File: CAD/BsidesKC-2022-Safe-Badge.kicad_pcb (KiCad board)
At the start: 2 copper layers, 104.1 x 121.5 mm, 7 parts

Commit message: WIP
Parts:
- removed the G*** at (0.00, 0.00) (x7)
- added G***: LOGO, LOGO, F.Cu at (12.8, 19.2)
- added G*** (x4): LOGO, LOGO, F.Cu at (147.9, 84.0)
- added G***: LOGO, LOGO, F.Cu at (21.1, 18.9)
- added G***: LOGO, LOGO, F.Cu at (19.1, 22.8)
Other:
- net class Default removed

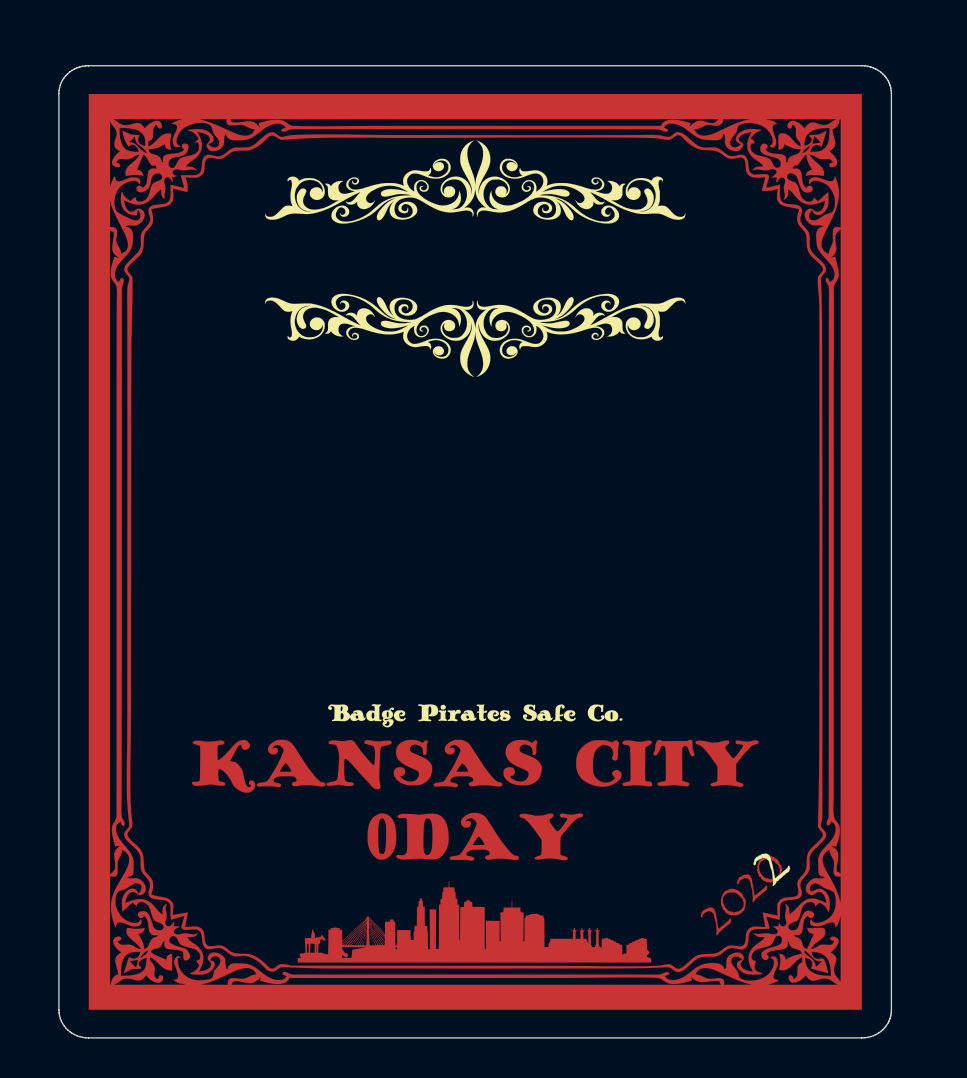
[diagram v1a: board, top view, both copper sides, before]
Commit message: adding and taking away
Adding electronics to boards, and removing old builds.
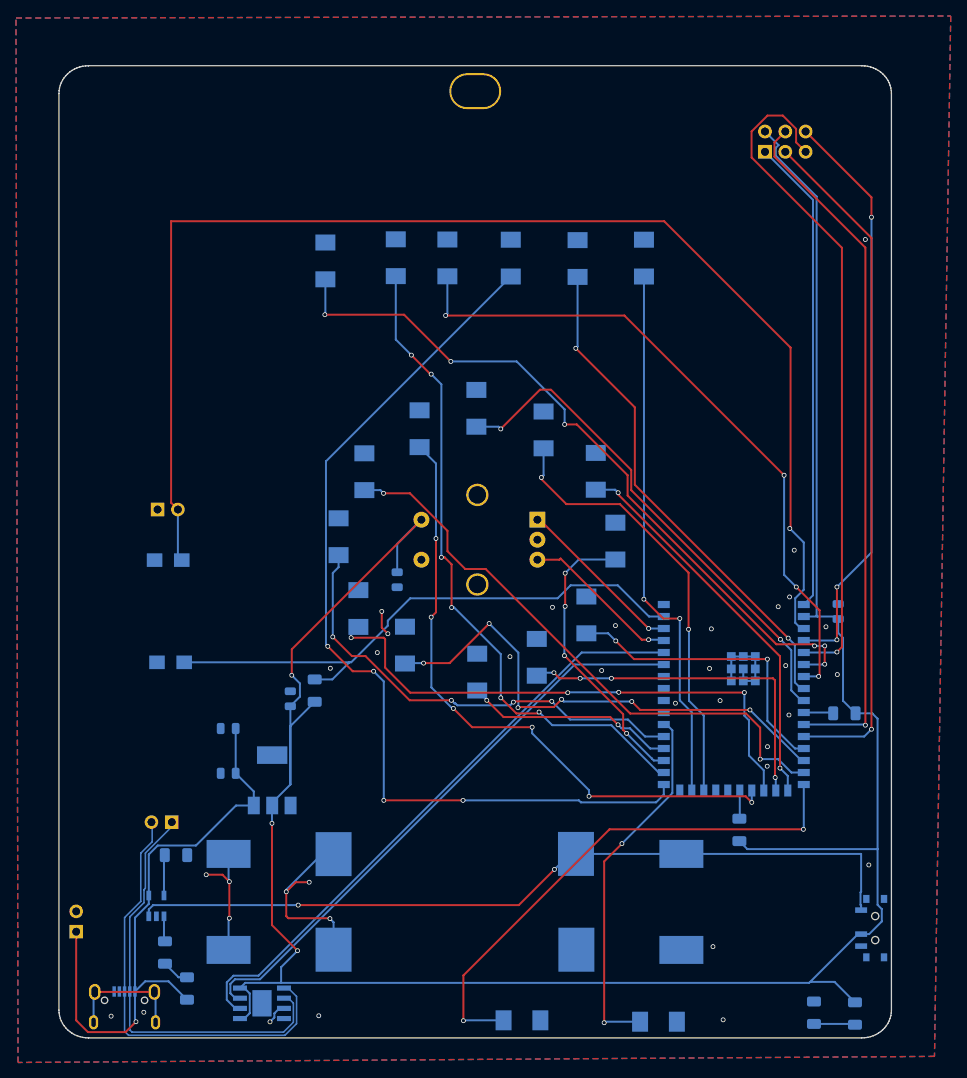
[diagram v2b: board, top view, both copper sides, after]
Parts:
- removed the G*** at (147.9, 84.0) (x2)
- added 1/0: SW_SPDT, BadgePiratesCommon:SW_SPDT_PCM12, B.Cu at (197.8, 135.3)
- added BT1: Battery, BadgePiratesCommon:AA, B.Cu at (145.6, 129.1)
- added C1: 1uF, BadgePiratesCommon:C_0805_2012Metric, B.Cu at (117.2, 110.4)
- added C2: 22uF, BadgePiratesCommon:C_0805_2012Metric, B.Cu at (193.4, 95.8)
- added C3: 0.1uF, BadgePiratesCommon:C_0805_2012Metric, B.Cu at (125.0, 106.7)
- added C4: .1uF, BadgePiratesCommon:C_0805_2012Metric, B.Cu at (138.3, 91.8)
- added C5: .1uF, BadgePiratesCommon:C_0805_2012Metric, B.Cu at (117.2, 116.0)
- added D- D+: Conn_01x02_Female, BadgePiratesCommon:PinHeader_1x02_P2.54mm_Vertical, B.Cu at (110.2, 122.1)
- added D1: LED, BadgePiratesCommon:LED_Osram_Lx_P47F_D2mm_ReverseMount_Proper_Mask Only, F.Cu at (129.3, 52.0)
- added D10: LED, BadgePiratesCommon:LED_Osram_Lx_P47F_D2mm_ReverseMount_Proper_Mask Only, F.Cu at (165.6, 87.0)
- added D11: LED, BadgePiratesCommon:LED_Osram_Lx_P47F_D2mm_ReverseMount_Proper_Mask Only, F.Cu at (162.0, 96.2)
- added D12: Charging LED, LED_SMD:LED_1206_3216Metric, B.Cu at (112.0, 142.9)
- added D13: LED, BadgePiratesCommon:LED_Osram_Lx_P47F_D2mm_ReverseMount_Proper_Mask Only, F.Cu at (155.8, 101.5)
- added D14: LED, BadgePiratesCommon:LED_Osram_Lx_P47F_D2mm_ReverseMount_Proper_Mask Only, F.Cu at (148.3, 103.3)
- added D15: LED, BadgePiratesCommon:LED_Osram_Lx_P47F_D2mm_ReverseMount_Proper_Mask Only, F.Cu at (139.3, 100.0)
- added D16: Pwr, LED_SMD:LED_1206_3216Metric, B.Cu at (190.4, 145.9)
- added D17: LED, BadgePiratesCommon:LED_Osram_Lx_P47F_D2mm_ReverseMount_Proper_Mask Only, F.Cu at (133.5, 95.4)
- added D18: LED, BadgePiratesCommon:LED_Osram_Lx_P47F_D2mm_ReverseMount_Proper_Mask Only, F.Cu at (131.0, 86.4)
- added D19: LED, BadgePiratesCommon:LED_Osram_Lx_P47F_D2mm_ReverseMount_Proper_Mask Only, F.Cu at (134.2, 78.3)
- added D2: LED, BadgePiratesCommon:LED_Osram_Lx_P47F_D2mm_ReverseMount_Proper_Mask Only, F.Cu at (138.2, 51.5)
- added D20: LED, BadgePiratesCommon:LED_Osram_Lx_P47F_D2mm_ReverseMount_Proper_Mask Only, F.Cu at (141.1, 72.9)
- added D21: LED, BadgePiratesCommon:LED_Osram_Lx_P47F_D2mm_ReverseMount_Proper_Mask Only, F.Cu at (171.0, 147.1)
- added D22: LED, BadgePiratesCommon:LED_Osram_Lx_P47F_D2mm_ReverseMount_Proper_Mask Only, F.Cu at (153.9, 146.9)
- added D3: LED, BadgePiratesCommon:LED_Osram_Lx_P47F_D2mm_ReverseMount_Proper_Mask Only, F.Cu at (144.6, 51.6)
- added D4: LED, BadgePiratesCommon:LED_Osram_Lx_P47F_D2mm_ReverseMount_Proper_Mask Only, F.Cu at (152.5, 51.6)
- added D5: LED, BadgePiratesCommon:LED_Osram_Lx_P47F_D2mm_ReverseMount_Proper_Mask Only, F.Cu at (160.9, 51.6)
- added D6: LED, BadgePiratesCommon:LED_Osram_Lx_P47F_D2mm_ReverseMount_Proper_Mask Only, F.Cu at (169.2, 51.6)
- added D7: LED, BadgePiratesCommon:LED_Osram_Lx_P47F_D2mm_ReverseMount_Proper_Mask Only, F.Cu at (148.2, 70.4)
- added D8: LED, BadgePiratesCommon:LED_Osram_Lx_P47F_D2mm_ReverseMount_Proper_Mask Only, F.Cu at (156.6, 73.1)
- added D9: LED, BadgePiratesCommon:LED_Osram_Lx_P47F_D2mm_ReverseMount_Proper_Mask Only, F.Cu at (163.2, 78.2)
- added ESP32-S2 ROVER: ESP32-S2-WROVER, BadgePiratesCommon:ESP32-S2-WROVER, B.Cu at (180.4, 106.0)
- added G***: LOGO, BadgePirateLogos:BadgePiratesURL_B.SLK, F.Cu at (101.6, 52.8)
- added G***: LOGO, BadgePirateLogos:shi%%y_B.SLK, F.Cu at (195.8, 41.4)
- added G***: fg, BadgePirateLogos:FG_B.SILK, F.Cu at (132.0, 39.0)
- added G***: pecord, BadgePirateLogos:pecord_B.SLK, F.Cu at (155.0, 40.5)
- added G***: NG_BSilk, BadgePirateLogos:NG_B.SLK, F.Cu at (167.5, 38.0)
- added G***: JiggleBilly, BadgePirateLogos:Jiggle_B.SLK, F.Cu at (143.2, 39.9)
- added G***: BP Logo, BadgePirateLogos:BPSkull_Distressed_B.SILK, F.Cu at (103.8, 36.8)
- added GND 5v: Conn_01x02_Female, BadgePiratesCommon:PinHeader_1x02_P2.54mm_Vertical, B.Cu at (98.2, 135.8)
- added J2: Conn_01x02_Female, BadgePiratesCommon:PinHeader_1x02_P2.54mm_Vertical, B.Cu at (108.4, 83.0)
- added J4: USB_B_Mini, BadgePiratesCommon:USB_Micro-B_Wuerth, B.Cu at (104.2, 145.2)
- added R1: 2k, BadgePiratesCommon:R_1206_3216Metric, B.Cu at (110.7, 126.2)
- added R2: 330, BadgePiratesCommon:R_1206_3216Metric, B.Cu at (109.3, 138.4)
- added R3: R, BadgePiratesCommon:R_1206_3216Metric, B.Cu at (195.6, 146.0)
- added R4: 1k, BadgePiratesCommon:R_1206_3216Metric, B.Cu at (128.0, 105.7)
- added R5: 10k, BadgePiratesCommon:R_1206_3216Metric, B.Cu at (181.1, 123.1)
- added R6: R_Small_US, BadgePiratesCommon:R_1206_3216Metric, B.Cu at (194.2, 108.5)
- added REF**: 6x4 SLOT, BadgePiratesCommon:Slot_6x4mm, F.Cu at (148.1, 30.7)
- added SW2: SW_SPST, BadgePiratesCommon:Switch_Tactile_SMD_B3U-1000P-BPVersion, B.Cu at (109.7, 89.3)
- added SW3: RotaryEncoder_Switch, Rotary_Encoder:RotaryEncoder_Alps_EC12E-Switch_Vertical_H20mm_CircularMountingHoles, B.Cu at (155.8, 84.3)
- added SW_Reset1: Reset_Btn, BadgePiratesCommon:Switch_Tactile_SMD_B3U-1000P-BPVersion, B.Cu at (110.0, 102.1)
- added U1: LTC4054, BadgePiratesCommon:LTC4054, B.Cu at (108.2, 132.6)
- added U3: CH330N, BadgePiratesCommon:SOIC-8-1EP_W3.9mm, B.Cu at (121.4, 144.8)
- added U4: TLV1117-33, BadgePiratesCommon:SOT-223, B.Cu at (122.7, 116.9)
- added X1: Badgelife_sao_connector_v169bis, BadgePiratesCommon:Badgelife-SAOv169-SAO_Side_B.SLK, F.Cu at (186.4, 37.1)
- added kibuzzard-62C2405D: G***, kibuzzard-62C2405D, B.Cu at (136.0, 29.6)
- added kibuzzard-62C240C4: G***, kibuzzard-62C240C4, B.Cu at (119.5, 38.9)
- moved G*** 82.5 mm to (95.0, 27.0)
- moved G*** 76.0 mm to (95.0, 27.0)
- moved G*** 74.3 mm to (95.0, 27.0)
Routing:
- net VCC: track 0.00 -> 310.9 mm, vias 0 -> 3
- net Boot: track 0.00 -> 163.9 mm, vias 0 -> 1
- net GND: track 0.00 -> 116.9 mm, vias 0 -> 35
- net IO33: track 0.00 -> 116.3 mm, vias 0 -> 4
- net Net-(BT1-Pad1): track 0.00 -> 99.9 mm, vias 0 -> 2
- net IO03: track 0.00 -> 91.6 mm, vias 0 -> 6
- net IO08: track 0.00 -> 87.2 mm, vias 0 -> 1
- net IO09: track 0.00 -> 85.5 mm, vias 0 -> 1
- net IO02: track 0.00 -> 84.6 mm, vias 0 -> 1
- net IO04: track 0.00 -> 84.5 mm, vias 0 -> 4
- net IO34: track 0.00 -> 83.0 mm, vias 0 -> 6
- net IO17: track 0.00 -> 79.6 mm, vias 0 -> 6
- net USB_TX_ESP_RX: track 0.00 -> 76.0 mm
- net VBUS: track 0.00 -> 75.6 mm, vias 0 -> 1
- net IO12: track 0.00 -> 73.3 mm, vias 0 -> 2
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- added copper zone on B.Cu, net GND
- added copper zone on F.Cu, net GND

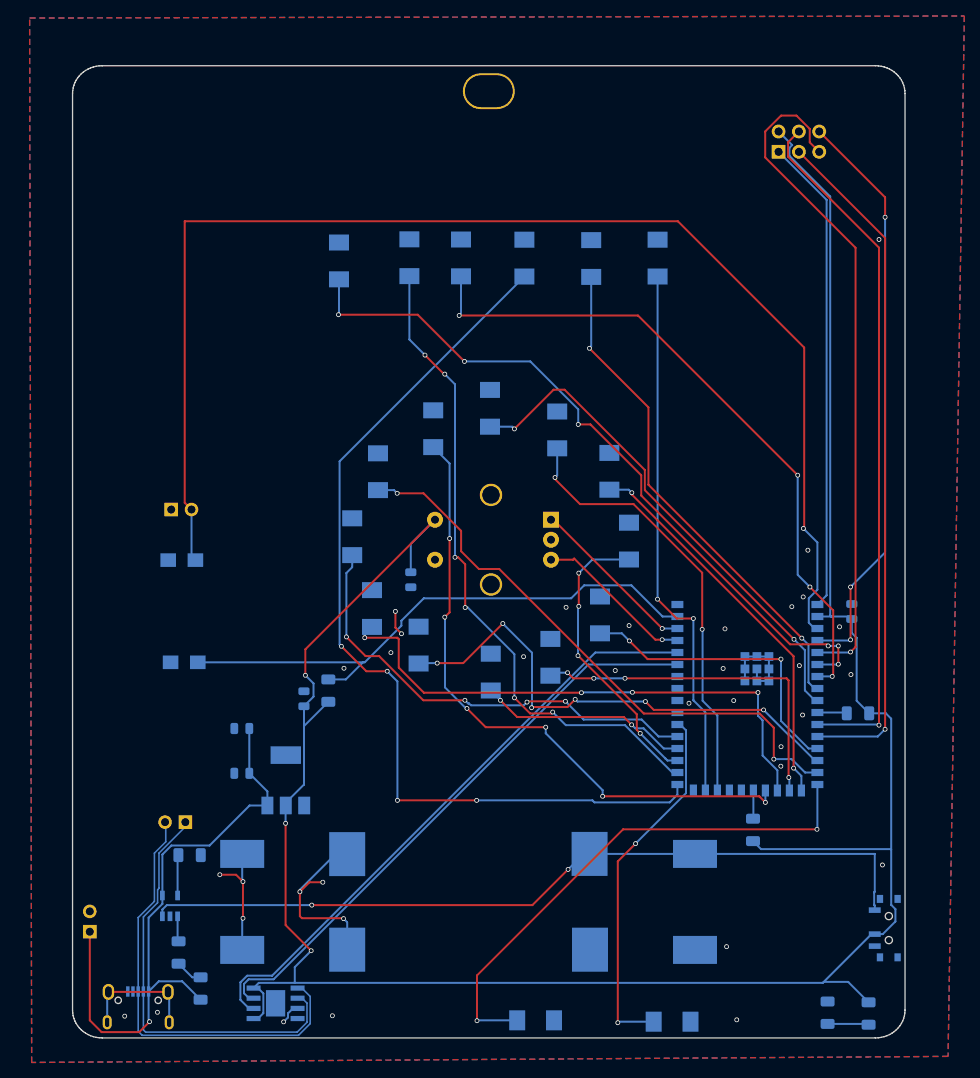
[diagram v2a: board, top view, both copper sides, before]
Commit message: fixing footprint and fill
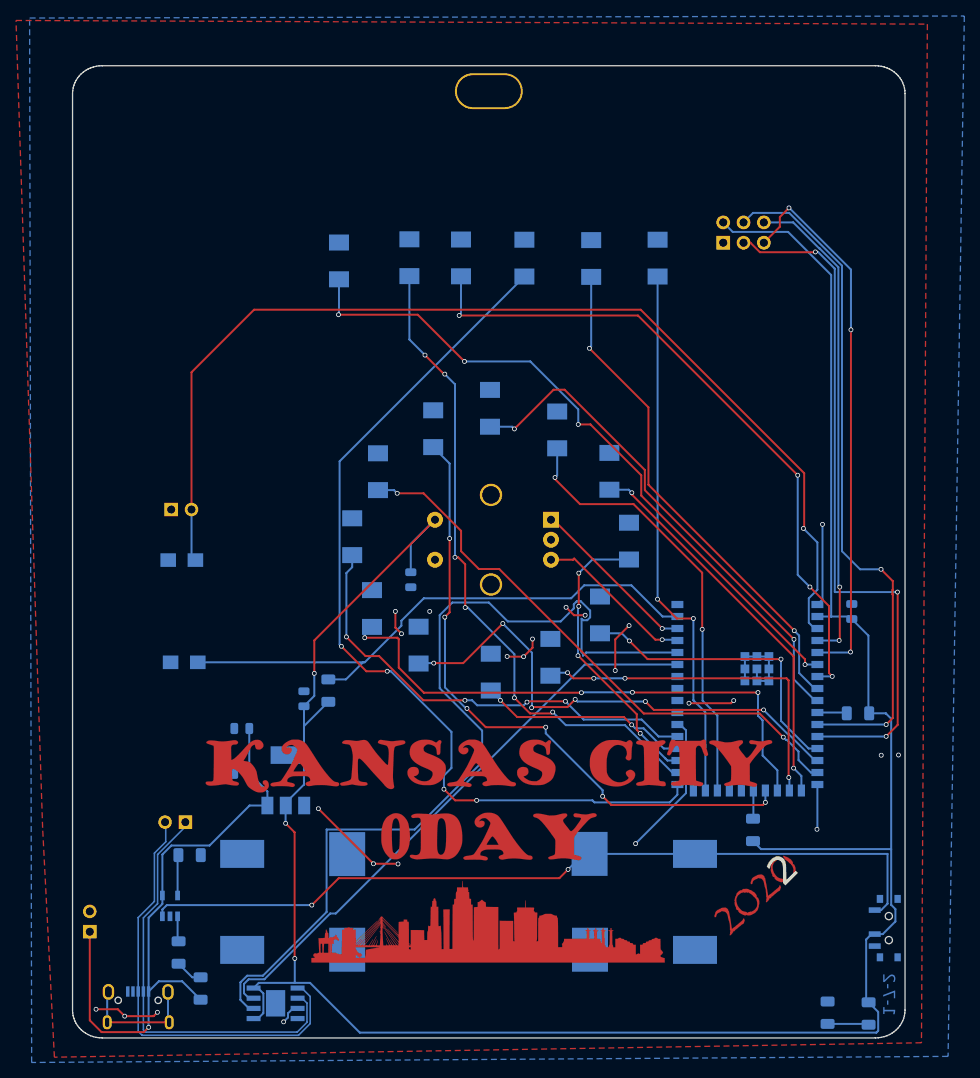
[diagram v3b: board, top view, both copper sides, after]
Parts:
- removed D21, D22: LED, BadgePiratesCommon:LED_Osram_Lx_P47F_D2mm_ReverseMount_Proper_Mask Only
- removed kibuzzard-62C2405D: G***, kibuzzard-62C2405D
- added G***: rixon, BadgePiratesLogo:rixon_B.SLK, F.Cu at (180.0, 38.4)
- added kibuzzard-62FC3E66: G***, kibuzzard-62FC3E66, B.Cu at (131.4, 30.8)
- ESP32-S2 ROVER: value ESP32-S2-WROVER -> ESP32-S2-WROOM
- GND 5v: value Conn_01x02_Female -> 1x2
- J2: value Conn_01x02_Female -> 1x2
- REF**: value 6x4 SLOT -> 8x4 SLOT
- SW2: value SW_SPST -> Boot Mode
- X1: value Badgelife_sao_connector_v169bis -> sao_v169bis
- moved G*** 22.9 mm to (179.7, 57.6)
- moved X1 13.3 mm to (179.5, 48.5)
- renumbered SW_Reset1 to Reset
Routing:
- net IO13: track 66.4 -> 5.62 mm, vias 2 -> 1
- net GND: track 116.9 -> 70.4 mm, vias 35 -> 21
- net USB_TX_ESP_RX: track 76.0 -> 113.6 mm
- net Boot: track 163.9 -> 133.2 mm
- net IO38: track 46.0 -> 18.2 mm, vias 2 -> 1
- net IO02: track 84.6 -> 68.6 mm, vias 1 -> 3
- net IO01: track 72.9 -> 61.1 mm, vias 3 -> 2
- net IO03: track 91.6 -> 85.4 mm, vias 6 -> 4
- net IO33: track 116.3 -> 113.2 mm
- net IO09: track 85.5 -> 88.3 mm, vias 1 -> 3
- net Net-(BT1-Pad1): track 99.9 -> 102.5 mm
- net IO12: track 73.3 -> 71.7 mm
- net IO08: track 87.2 -> 86.0 mm, vias 1 -> 2
- net unconnected-(J4-Pad6): track 15.2 -> 16.0 mm
- net (no net): vias 0 -> 1
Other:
- board text added: "1-7-2"
- board text added: "2"
